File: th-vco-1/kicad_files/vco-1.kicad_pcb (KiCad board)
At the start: 2 copper layers, 76.2 x 100.3 mm, 73 parts, among them J1 PWM, J2 1V/OCT, J3 EXP FM, J4 LIN FM, J5 POWER, J6 PULSE, J7 SINE, J8 TRIANGLE, Q1 2N3906, Q2 2N3906, Q3 2N3904, Q4 2N3904, Q5 2N3904, Q6 2N3904, U1 TL072, U2 CA3080, U3 TL072, U4 TL072

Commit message: Update PCB with initial 12 V values
And add PCB layout pdf.
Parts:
- R20: value 20k -> 24k
- R26: value 100k -> 110k
- R28: value 5.1k -> 3.9k
- R30, R33: value 12k -> 14k
- R35: value 3k -> 2k
- R36: value 1.8k -> 2k
- R6: value 1.5M -> 1.2M
- R8: value 2k -> 2k ther
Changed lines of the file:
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@@
       (effects (font (size 1 1) (thickness 0.15)))
     )
-    (fp_text value 1.5M (at 5.08 0) (layer F.Fab)
+    (fp_text value 1.2M (at 5.08 0) (layer F.Fab)
       (effects (font (size 1 1) (thickness 0.15)))
     )
@@
       (effects (font (size 1 1) (thickness 0.15)))
     )
-    (fp_text value 2k (at 5.08 0 90) (layer F.Fab)
+    (fp_text value "2k ther" (at 5.08 0 90) (layer F.Fab)
       (effects (font (size 1 1) (thickness 0.15)))
     )
@@
       (effects (font (size 1 1) (thickness 0.15)))
     )
-    (fp_text value 20k (at 7.62 0 180) (layer F.Fab)
+    (fp_text value 24k (at 7.62 0 180) (layer F.Fab)
       (effects (font (size 1 1) (thickness 0.15)))
     )
@@
       (effects (font (size 1 1) (thickness 0.15)))
     )
-    (fp_text value 100k (at 7.62 0 270) (layer F.Fab)
+    (fp_text value 110k (at 7.62 0 270) (layer F.Fab)
       (effects (font (size 1 1) (thickness 0.15)))
     )
@@
       (effects (font (size 1 1) (thickness 0.15)))
     )
-    (fp_text value 5.1k (at 7.62 0 180) (layer F.Fab)
+    (fp_text value 3.9k (at 7.62 0 180) (layer F.Fab)
       (effects (font (size 1 1) (thickness 0.15)))
     )
@@
       (effects (font (size 1 1) (thickness 0.15)))
     )
-    (fp_text value 12k (at 8.89 0 270) (layer F.Fab)
+    (fp_text value 14k (at 8.89 0 270) (layer F.Fab)
       (effects (font (size 1 1) (thickness 0.15)))
     )
@@
       (effects (font (size 1 1) (thickness 0.15)))
     )
-    (fp_text value 12k (at 8.89 0 270) (layer F.Fab)
+    (fp_text value 14k (at 8.89 0 270) (layer F.Fab)
       (effects (font (size 1 1) (thickness 0.15)))
     )
@@
       (effects (font (size 1 1) (thickness 0.15)))
     )
-    (fp_text value 3k (at 8.89 0 180) (layer F.Fab)
+    (fp_text value 2k (at 8.89 0 180) (layer F.Fab)
       (effects (font (size 1 1) (thickness 0.15)))
     )
@@
       (effects (font (size 1 1) (thickness 0.15)))
     )
-    (fp_text value 1.8k (at 8.89 0 180) (layer F.Fab)
-      (effects (font (size 1 1) (thickness 0.15)))
-    )
+    (fp_text value 2k (at 8.89 0 180) (layer F.Fab)
+      (effects (font (size 1 1) (thickness 0.15)))
+    )

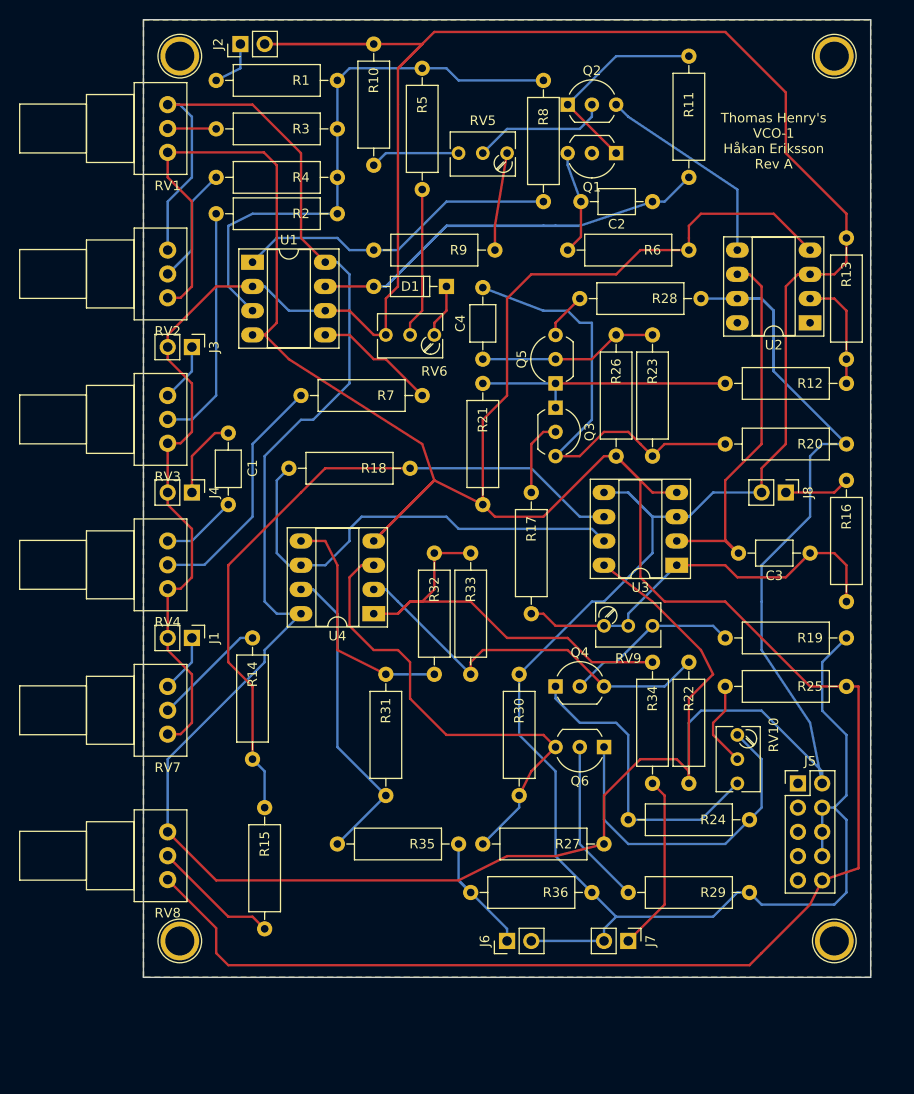
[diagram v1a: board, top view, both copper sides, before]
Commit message: Update after rev A failure
Fixed most of the errors found in rev A. No fix for the
reverse pots, though, since I don't know how.
At this point it would also mean to re-CAD, not too happy
about that.
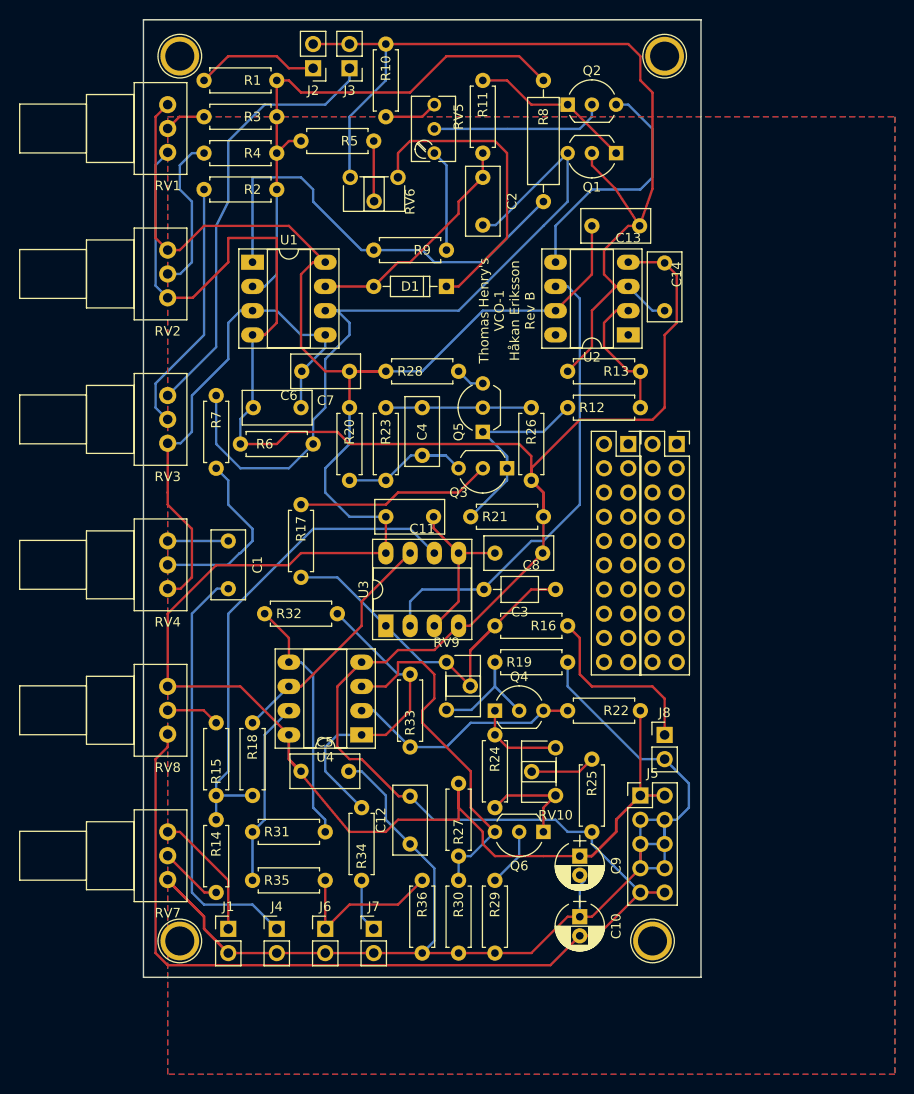
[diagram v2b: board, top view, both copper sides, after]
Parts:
- added ?: , Socket_Strips:Socket_Strip_Straight_2x10_Pitch2.54mm, F.Cu at (186.7, 71.1)
- added ?: , Socket_Strips:Socket_Strip_Straight_2x10_Pitch2.54mm, F.Cu at (191.8, 71.1)
- added C10: 10uF, Capacitors_THT:CP_Radial_D5.0mm_P2.00mm, F.Cu at (181.6, 120.7)
- added C11: 10nF, Capacitors_THT:C_Rect_L7.2mm_W3.5mm_P5.00mm_FKS2_FKP2_MKS2_MKP2, F.Cu at (161.3, 78.7)
- added C12: 10nF, Capacitors_THT:C_Rect_L7.2mm_W3.5mm_P5.00mm_FKS2_FKP2_MKS2_MKP2, F.Cu at (163.8, 113.0)
- added C13: 10nF, Capacitors_THT:C_Rect_L7.2mm_W3.5mm_P5.00mm_FKS2_FKP2_MKS2_MKP2, F.Cu at (182.9, 48.3)
- added C14: 10nF, Capacitors_THT:C_Rect_L7.2mm_W3.5mm_P5.00mm_FKS2_FKP2_MKS2_MKP2, F.Cu at (190.5, 57.1)
- added C5: 10nF, Capacitors_THT:C_Rect_L7.2mm_W3.5mm_P5.00mm_FKS2_FKP2_MKS2_MKP2, F.Cu at (152.4, 105.4)
- added C6: 10nF, Capacitors_THT:C_Rect_L7.2mm_W3.5mm_P5.00mm_FKS2_FKP2_MKS2_MKP2, F.Cu at (152.4, 67.3)
- added C7: 10nF, Capacitors_THT:C_Rect_L7.2mm_W3.5mm_P5.00mm_FKS2_FKP2_MKS2_MKP2, F.Cu at (157.5, 63.5)
- added C8: 10nF, Capacitors_THT:C_Rect_L7.2mm_W3.5mm_P5.00mm_FKS2_FKP2_MKS2_MKP2, F.Cu at (172.7, 82.5)
- added C9: 10uF, Capacitors_THT:CP_Radial_D5.0mm_P2.00mm, F.Cu at (181.6, 114.3)
- C1, C2, C4: footprint Capacitors_THT:C_Axial_L3.8mm_D2.6mm_P7.50mm_Horizontal -> Capacitors_THT:C_Rect_L7.2mm_W3.5mm_P5.00mm_FKS2_FKP2_MKS2_MKP2
- C3: value 1n -> 1n polystyrene
- J5: value POWER -> EURORACK POWER
- R1, R2, R3: value 100 -> 100k; footprint Resistors_THT:R_Axial_DIN0309_L9.0mm_D3.2mm_P12.70mm_Horizontal -> Resistors_THT:R_Axial_DIN0207_L6.3mm_D2.5mm_P7.62mm_Horizontal
- R10, R11, R12, R13, R14, R15, R16, R17, R18, R19, R20, R21, R22, R23, R24, R25, R26, R27, R28, R29, R30, R31, R32, R33, R34, R35, R36, R4, R5, R6, R7, R9: footprint Resistors_THT:R_Axial_DIN0309_L9.0mm_D3.2mm_P12.70mm_Horizontal -> Resistors_THT:R_Axial_DIN0207_L6.3mm_D2.5mm_P7.62mm_Horizontal
- R8: value 2k ther -> 2k therm
- RV10, RV6, RV9: footprint Potentiometers:Potentiometer_Trimmer_Bourns_3266Y -> Potentiometers:Potentiometer_Trimmer_ACP_CA6h_Vertical
- moved R20 52.2 mm to (157.5, 67.3), turned to 270 degrees
- moved J4 46.6 mm to (149.9, 121.9), turned to 0 degrees
- moved R28 33.9 mm to (161.3, 63.5), turned to 0 degrees
- moved J3 33.6 mm to (157.5, 31.8), turned to 180 degrees
- moved R6 33.5 mm to (153.7, 71.1), turned to 180 degrees
- moved R16 32.9 mm to (180.3, 90.2), turned to 180 degrees
- moved R34 32.1 mm to (158.8, 116.8)
- moved U3 31.1 mm to (161.3, 90.2), turned to 90 degrees
- moved J1 30.7 mm to (144.8, 121.9), turned to 0 degrees
- moved R30 29.9 mm to (168.9, 124.5), turned to 90 degrees
- moved R23 29.0 mm to (161.3, 67.3)
- moved J8 28.4 mm to (190.5, 101.6), turned to 0 degrees
- moved C3 26.9 mm to (179.1, 86.4)
- moved R18 26.9 mm to (147.3, 100.3), turned to 270 degrees
- moved J7 26.7 mm to (160.0, 121.9), turned to 0 degrees
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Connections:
- J5 pad 1: (no net) -> +12V
- J5 pad 3: (no net) -> GND
- J5 pad 5: (no net) -> GND
- J5 pad 7: (no net) -> GND
- J5 pad 9: (no net) -> -12V
- R7 pad 1: Net-(R7-Pad1) -> Net-(C2-Pad2)
- U1 pad 2: GND -> Net-(R1-Pad1)
- U1 pad 3: Net-(R1-Pad1) -> GND
- U1 pad 5: Net-(R7-Pad1) -> GND
- U1 pad 6: GND -> Net-(C2-Pad2)
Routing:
- net +12V: track 319.3 -> 245.2 mm
- net Net-(C2-Pad2): track 11.0 -> 81.9 mm
- net GND: track 380.8 -> 321.4 mm
- net Net-(C2-Pad1): track 65.1 -> 24.5 mm
- net Net-(J3-Pad1): track 6.13 -> 45.7 mm
- net Net-(C1-Pad2): track 8.62 -> 44.6 mm
- net Net-(C4-Pad2): track 48.4 -> 15.5 mm
- net -12V: track 326.1 -> 295.0 mm
- net Net-(D1-Pad1): track 5.61 -> 32.4 mm
- net Net-(Q6-Pad1): track 35.4 -> 11.2 mm
- net Net-(Q4-Pad1): track 32.4 -> 9.45 mm
- net Net-(R18-Pad1): track 48.1 -> 25.4 mm
- net Net-(R14-Pad1): track 72.7 -> 52.3 mm
- net Net-(Q4-Pad3): track 41.1 -> 24.7 mm
- net Net-(R31-Pad1): track 33.2 -> 19.4 mm
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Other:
- board size 76.2 x 100.3 mm -> 58.4 x 100.3 mm
- board text added: "Thomas Henry's VCO-1 Håkan Eriksson Rev B"
- board text removed: "Thomas Henry's VCO-1 Håkan Eriksson Rev A"

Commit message: Use 16 pole power connector
Even though a 10 pole would be enough, my current plan is
to use 16 pole for all boards, thus minimizing cost for
power connectors/cables.

Possibly a bad idea, but if I will go through with the plans
to run workshops using these boards, there will be a LOT of
component bought, and it makes sense to keep cost down.
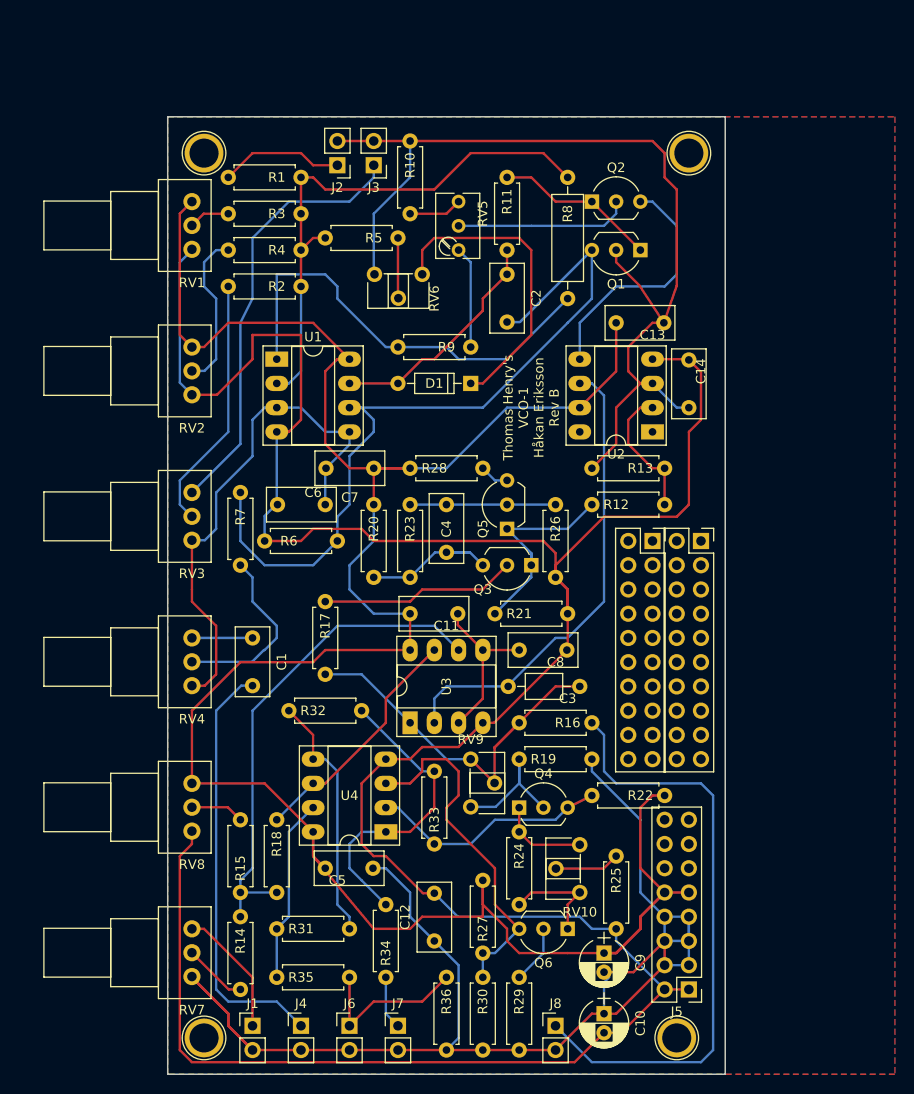
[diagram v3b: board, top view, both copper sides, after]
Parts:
- J5: value EURORACK POWER -> EURO_POWER; footprint Pin_Headers:Pin_Header_Straight_2x05_Pitch2.54mm -> Pin_Headers:Pin_Header_Straight_2x08_Pitch2.54mm
- R8: value 2k therm -> 2k +3500ppm/C thermistor
- moved J8 32.6 mm to (179.1, 132.1)
- moved J5 20.9 mm to (193.0, 128.3), turned to 180 degrees
- moved C11 10.5 mm to (163.8, 88.9)
- moved Q5 10.5 mm to (174.0, 80.0)
- moved R14 10.5 mm to (146.1, 120.7)
- moved C2 10.5 mm to (174.0, 53.3)
- moved J1 10.5 mm to (147.3, 132.1)
- moved J4 10.5 mm to (152.4, 132.1)
- moved J6 10.5 mm to (157.5, 132.1)
- moved J7 10.5 mm to (162.6, 132.1)
- moved R10 10.5 mm to (163.8, 47.0)
- moved R21 10.5 mm to (172.7, 88.9)
- moved R30 10.5 mm to (171.4, 134.6)
- moved R36 10.5 mm to (167.6, 134.6)
- moved RV8 10.5 mm to (141.0, 106.7)
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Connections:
- J5 pad 1: +12V -> -12V
- J5 pad 10: -12V -> +12V
- J5 pad 2: +12V -> -12V
- J5 pad 9: -12V -> +12V
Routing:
- net Net-(J8-Pad1): track 19.4 -> 63.4 mm
- net +12V: track 245.2 -> 249.3 mm
- net GND: track 321.4 -> 323.7 mm
